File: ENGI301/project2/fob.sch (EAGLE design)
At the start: 21 parts, among them SW1 PUSH_BUTTON, SW2 PUSH_BUTTON, SW3 PUSH_BUTTON, SW4 PUSH_BUTTON

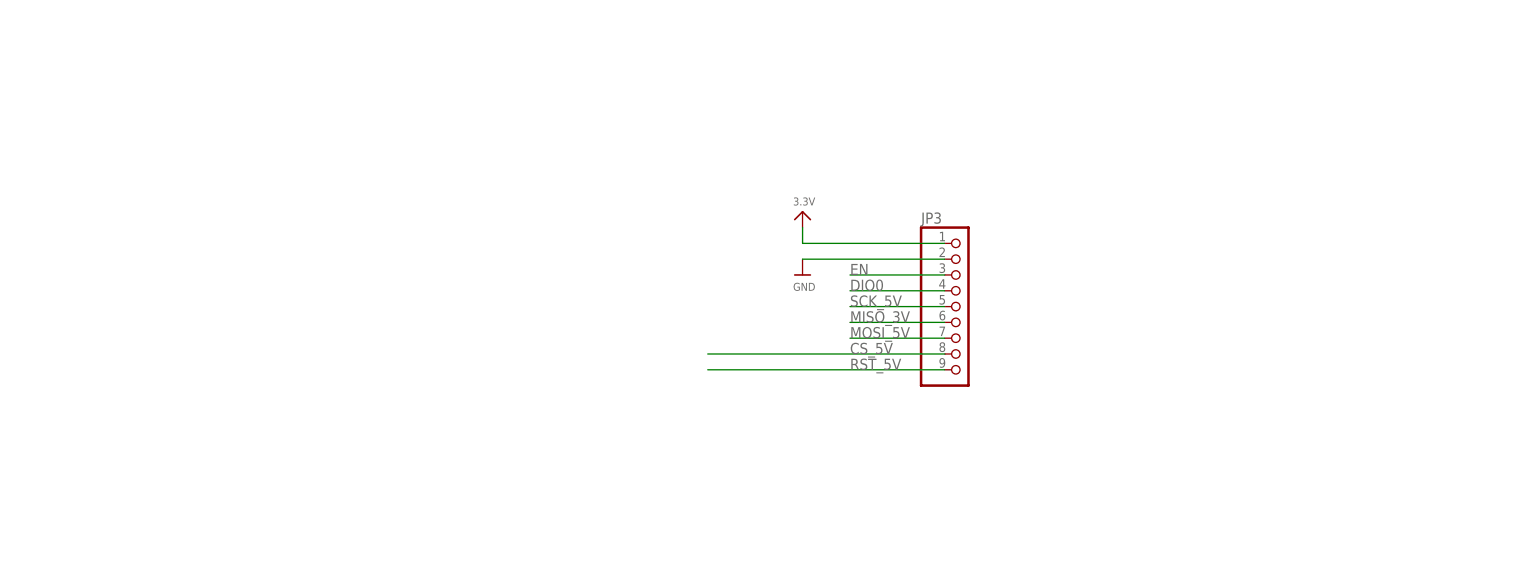
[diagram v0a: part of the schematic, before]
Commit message: added to PCB design
- mounting holes
- documentation
- titles and stuff
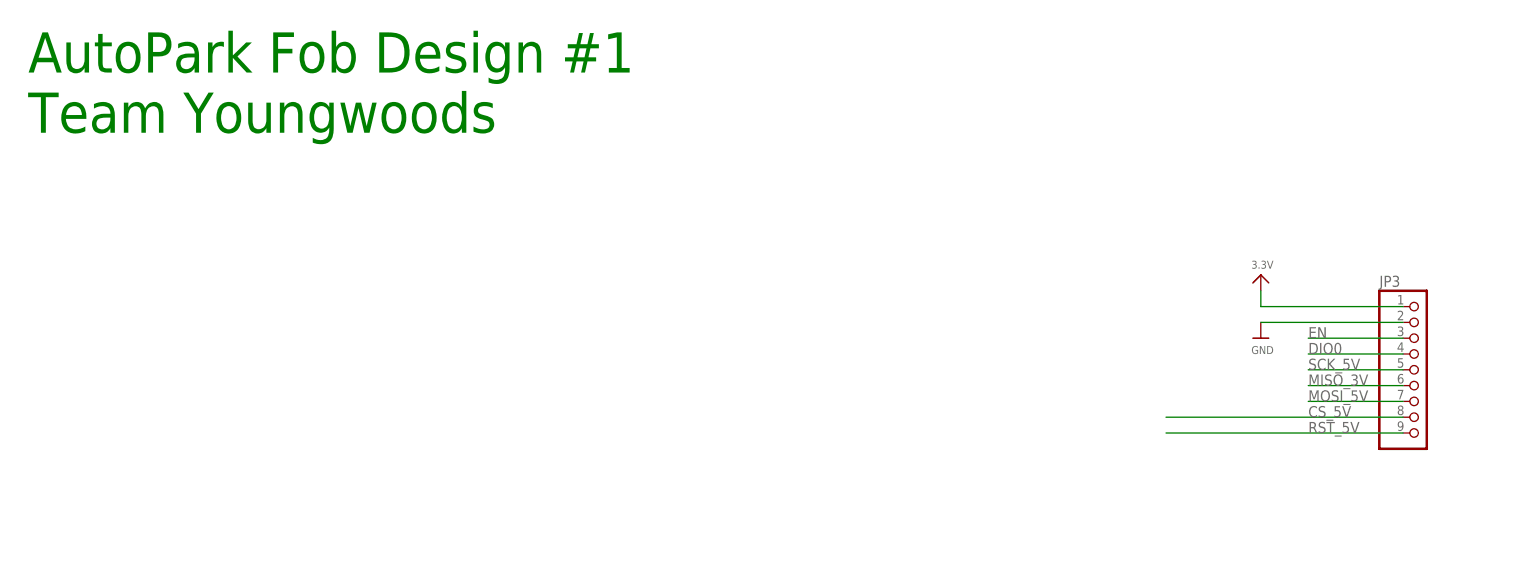
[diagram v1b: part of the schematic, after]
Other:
- note added: "AutoPark Fob Design #1 Team Youngwoods"
- moved on the sheet: JP3
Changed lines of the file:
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@@
 <text x="279.4" y="144.78" size="5.08" layer="91">Power Source</text>
 <text x="332.74" y="40.64" size="1.778" layer="91">Eunice Tan</text>
+<text x="0" y="248.92" size="6.4516" layer="91">AutoPark Fob Design #1
+Team Youngwoods</text>
 </plain>
 <instances>
@@
 <attribute name="VALUE" x="210.82" y="76.2" size="1.778" layer="96"/>
 </instance>
-<instance part="JP3" gate="A" x="149.86" y="220.98" smashed="yes">
-<attribute name="NAME" x="143.51" y="234.315" size="1.778" layer="95"/>
-<attribute name="VALUE" x="143.51" y="205.74" size="1.778" layer="96"/>
-</instance>
-<instance part="U$18" gate="G$1" x="124.46" y="226.06" smashed="yes">
-<attribute name="VALUE" x="122.936" y="223.52" size="1.27" layer="96"/>
+<instance part="JP3" gate="A" x="223.52" y="210.82" smashed="yes">
+<attribute name="NAME" x="217.17" y="224.155" size="1.778" layer="95"/>
+<attribute name="VALUE" x="217.17" y="195.58" size="1.778" layer="96"/>
+</instance>
+<instance part="U$18" gate="G$1" x="198.12" y="215.9" smashed="yes">
+<attribute name="VALUE" x="196.596" y="213.36" size="1.27" layer="96"/>
 </instance>
 <instance part="LED1" gate="G$1" x="119.38" y="119.38" smashed="yes">
@@
 <attribute name="VALUE" x="229.616" y="94.996" size="1.27" layer="96"/>
 </instance>
-<instance part="U$13" gate="G$1" x="124.46" y="236.22" smashed="yes">
-<attribute name="VALUE" x="122.936" y="237.236" size="1.27" layer="96"/>
+<instance part="U$13" gate="G$1" x="198.12" y="226.06" smashed="yes">
+<attribute name="VALUE" x="196.596" y="227.076" size="1.27" layer="96"/>
 </instance>
 <instance part="U$2" gate="G$1" x="33.02" y="127" smashed="yes">
@@
 <pinref part="U$18" gate="G$1" pin="GND"/>
 <pinref part="JP3" gate="A" pin="2"/>
-<wire x1="124.46" y1="228.6" x2="147.32" y2="228.6" width="0.1524" layer="91"/>
+<wire x1="198.12" y1="218.44" x2="220.98" y2="218.44" width="0.1524" layer="91"/>
 </segment>
 <segment>
@@
 <segment>
 <pinref part="JP3" gate="A" pin="1"/>
-<wire x1="124.46" y1="233.68" x2="124.46" y2="231.14" width="0.1524" layer="91"/>
-<wire x1="124.46" y1="231.14" x2="147.32" y2="231.14" width="0.1524" layer="91"/>
+<wire x1="198.12" y1="223.52" x2="198.12" y2="220.98" width="0.1524" layer="91"/>
+<wire x1="198.12" y1="220.98" x2="220.98" y2="220.98" width="0.1524" layer="91"/>
 <pinref part="U$13" gate="G$1" pin="3.3V"/>
 </segment>
@@
 <net name="RST_5V" class="0">
 <segment>
-<label x="132.08" y="210.82" size="1.778" layer="95"/>
+<label x="205.74" y="200.66" size="1.778" layer="95"/>
 <pinref part="JP3" gate="A" pin="9"/>
-<wire x1="109.22" y1="210.82" x2="147.32" y2="210.82" width="0.1524" layer="91"/>
+<wire x1="182.88" y1="200.66" x2="220.98" y2="200.66" width="0.1524" layer="91"/>
 </segment>
 <segment>
@@
 <net name="MOSI_5V" class="0">
 <segment>
-<wire x1="147.32" y1="215.9" x2="132.08" y2="215.9" width="0.1524" layer="91"/>
-<label x="132.08" y="215.9" size="1.778" layer="95"/>
+<wire x1="220.98" y1="205.74" x2="205.74" y2="205.74" width="0.1524" layer="91"/>
+<label x="205.74" y="205.74" size="1.778" layer="95"/>
 <pinref part="JP3" gate="A" pin="7"/>
 </segment>
@@
 <net name="SCK_5V" class="0">
 <segment>
-<wire x1="147.32" y1="220.98" x2="132.08" y2="220.98" width="0.1524" layer="91"/>
-<label x="132.08" y="220.98" size="1.778" layer="95"/>
+<wire x1="220.98" y1="210.82" x2="205.74" y2="210.82" width="0.1524" layer="91"/>
+<label x="205.74" y="210.82" size="1.778" layer="95"/>
 <pinref part="JP3" gate="A" pin="5"/>
 </segment>
@@
 <net name="CS_5V" class="0">
 <segment>
-<label x="132.08" y="213.36" size="1.778" layer="95"/>
+<label x="205.74" y="203.2" size="1.778" layer="95"/>
 <pinref part="JP3" gate="A" pin="8"/>
-<wire x1="109.22" y1="213.36" x2="147.32" y2="213.36" width="0.1524" layer="91"/>
+<wire x1="182.88" y1="203.2" x2="220.98" y2="203.2" width="0.1524" layer="91"/>
 </segment>
 <segment>
@@
 <net name="MISO_3V" class="0">
 <segment>
-<wire x1="147.32" y1="218.44" x2="132.08" y2="218.44" width="0.1524" layer="91"/>
-<label x="132.08" y="218.44" size="1.778" layer="95"/>
+<wire x1="220.98" y1="208.28" x2="205.74" y2="208.28" width="0.1524" layer="91"/>
+<label x="205.74" y="208.28" size="1.778" layer="95"/>
 <pinref part="JP3" gate="A" pin="6"/>
 </segment>
@@
 <net name="EN" class="0">
 <segment>
-<wire x1="147.32" y1="226.06" x2="132.08" y2="226.06" width="0.1524" layer="91"/>
-<label x="132.08" y="226.06" size="1.778" layer="95"/>
+<wire x1="220.98" y1="215.9" x2="205.74" y2="215.9" width="0.1524" layer="91"/>
+<label x="205.74" y="215.9" size="1.778" layer="95"/>
 <pinref part="JP3" gate="A" pin="3"/>
 </segment>
@@
 <net name="DIO0" class="0">
 <segment>
-<wire x1="147.32" y1="223.52" x2="132.08" y2="223.52" width="0.1524" layer="91"/>
-<label x="132.08" y="223.52" size="1.778" layer="95"/>
+<wire x1="220.98" y1="213.36" x2="205.74" y2="213.36" width="0.1524" layer="91"/>
+<label x="205.74" y="213.36" size="1.778" layer="95"/>
 <pinref part="JP3" gate="A" pin="4"/>
 </segment>
@@
 </drawing>
 <compatibility>
+<note version="6.3" minversion="6.2.2" severity="warning">
+Since Version 6.2.2 text objects can contain more than one line,
+which will not be processed correctly with this version.
+</note>
 <note version="8.2" severity="warning">
 Since Version 8.2, EAGLE supports online libraries. The ids
